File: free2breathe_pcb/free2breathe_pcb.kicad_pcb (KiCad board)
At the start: 2 copper layers, 98 parts, among them J1 LED_Connector, J2 Alarm_Connector, J3 USB4110-GF-A_REVB, Q1 DMN3404L, Q2 AO3401A, SW1 Power_Switch, U1 IP5328, U2 MCP6044-E/P, U3 CO Sensor, U4 MCP6044-E/P, U5 SO2 Sensor, U6 MCP6044-E/P, U7 O3 Sensor, U8 MCP6044-E/P, U9 NO2 Sensor

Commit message: group sensors with supporting hardware
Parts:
- removed D9: LED, LED_SMD:LED_0603_1608Metric
- removed the R8 at (89.7, 96.5)
- D1, D2, D3, D4: footprint LED_THT:LED_D4.0mm -> LED_THT:LED_D3.0mm
- D5: renamed from D7; footprint LED_SMD:LED_0603_1608Metric -> LED_THT:LED_D3.0mm
- D6: renamed from D8; footprint LED_SMD:LED_0603_1608Metric -> LED_THT:LED_D3.0mm
- D7: renamed from D5; footprint LED_SMD:LED_0603_1608Metric -> LED_THT:LED_D3.0mm
- D8: renamed from D6; footprint LED_SMD:LED_0603_1608Metric -> LED_THT:LED_D3.0mm
- moved R22 131.9 mm to (191.4, 151.5), turned to -90 degrees
- moved BT3 129.7 mm to (148.5, 156.9)
- moved R20 127.2 mm to (191.4, 155.3), turned to -90 degrees
- moved R15 117.8 mm to (191.4, 147.7), turned to -90 degrees
- moved R19 114.1 mm to (258.5, 159.1), turned to 90 degrees
- moved R18 110.9 mm to (210.4, 159.5), turned to 90 degrees
- moved R21 105.9 mm to (240.2, 155.7), turned to -90 degrees
- moved R17 105.0 mm to (240.2, 147.5), turned to -90 degrees
- moved R34 104.6 mm to (192.4, 126.4), turned to -90 degrees
- moved R13 104.4 mm to (240.2, 152.0), turned to 90 degrees
- moved R29 104.1 mm to (192.2, 117.8), turned to 90 degrees
- moved R16 101.9 mm to (244.8, 147.5), turned to -90 degrees
- moved C24 101.5 mm to (196.0, 151.5), turned to 90 degrees
- moved R14 99.1 mm to (258.3, 141.3), turned to -90 degrees
- moved R31 98.2 mm to (211.6, 127.9), turned to 90 degrees
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- renumbered C2 to C1, C14 to C10, C16 to C11, C8 to C12, C1 to C13, C11 to C14, C13 to C15, C15 to C16, C25 to C18, C24 to C19, C5 to C2, C18 to C21, C23 to C22, C22 to C23, C21 to C24, C32 to C25, C33 to C27, C30 to C29, C6 to C3, C27 to C30, C29 to C32, C3 to C4, C4 to C5, C7 to C6, C9 to C7, C10 to C8, C12 to C9, J3 to J1, J1 to J2, J2 to J3, Q2 to Q1, Q1 to Q2, R9 to R10, R4 to R11, R27 to R12, R12 to R13, R26 to R14, R16 to R15, R14 to R16, R13 to R17, R25 to R18, R20 to R19, R3 to R2, R19 to R20, R18 to R21, R17 to R22, R2 to R23, R10 to R24, R11 to R25, R42 to R26, R43 to R27, R34 to R28, R36 to R29, R5 to R3, R40 to R30, R41 to R31, R38 to R32, R35 to R33, R39 to R34, R37 to R35, R21 to R4, R22 to R5, R23 to R6, R24 to R8, R6 to R9, U4 to U2, U2 to U3, U5 to U4, U3 to U5
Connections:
- U1 pad 20: Net-(U1-Pad20) -> unconnected-(U1-Pad20)
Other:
- board outline added: 63.5 x 127 mm

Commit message: begin board layout
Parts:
- moved BT1 235.2 mm to (274.4, 83.1)
- moved SW1 227.3 mm to (246.3, 25.2), turned to -90 degrees
- moved BT2 176.6 mm to (274.5, 95.4)
- moved U1 175.4 mm to (247.0, 99.0), turned to -90 degrees
- moved C14 168.4 mm to (269.3, 99.4), turned to -90 degrees
- moved C15 166.0 mm to (267.5, 99.5), turned to -90 degrees
- moved C16 163.6 mm to (265.7, 99.5), turned to -90 degrees
- moved C17 161.3 mm to (263.9, 99.5), turned to -90 degrees
- moved D8 155.8 mm to (247.6, 119.7)
- moved L1 155.6 mm to (258.4, 99.0), turned to 90 degrees
- moved C12 154.9 mm to (253.8, 101.0), turned to -90 degrees
- moved D7 153.5 mm to (244.7, 119.7), turned to 180 degrees
- moved BT3 152.5 mm to (274.4, 70.8)
- moved J1 151.7 mm to (221.2, 96.8), turned to -90 degrees
- moved D6 151.7 mm to (247.6, 114.7)
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
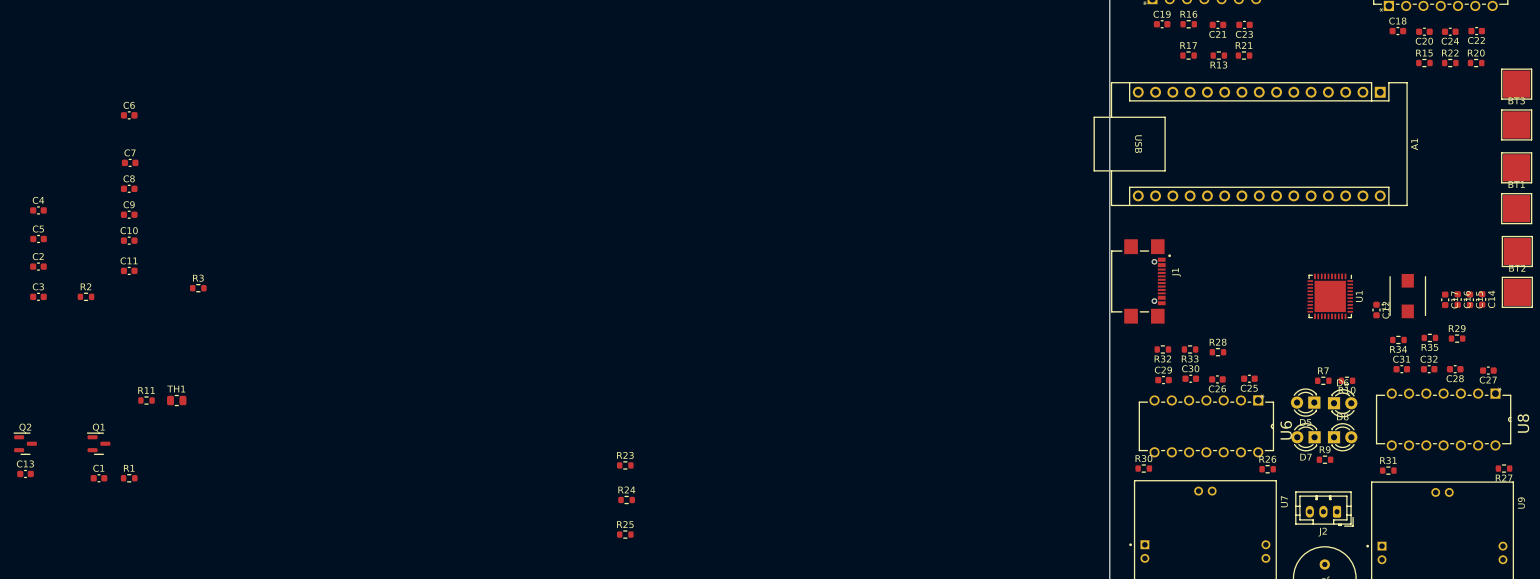
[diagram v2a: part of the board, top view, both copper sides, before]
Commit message: rest of components placed in board (very poorly)
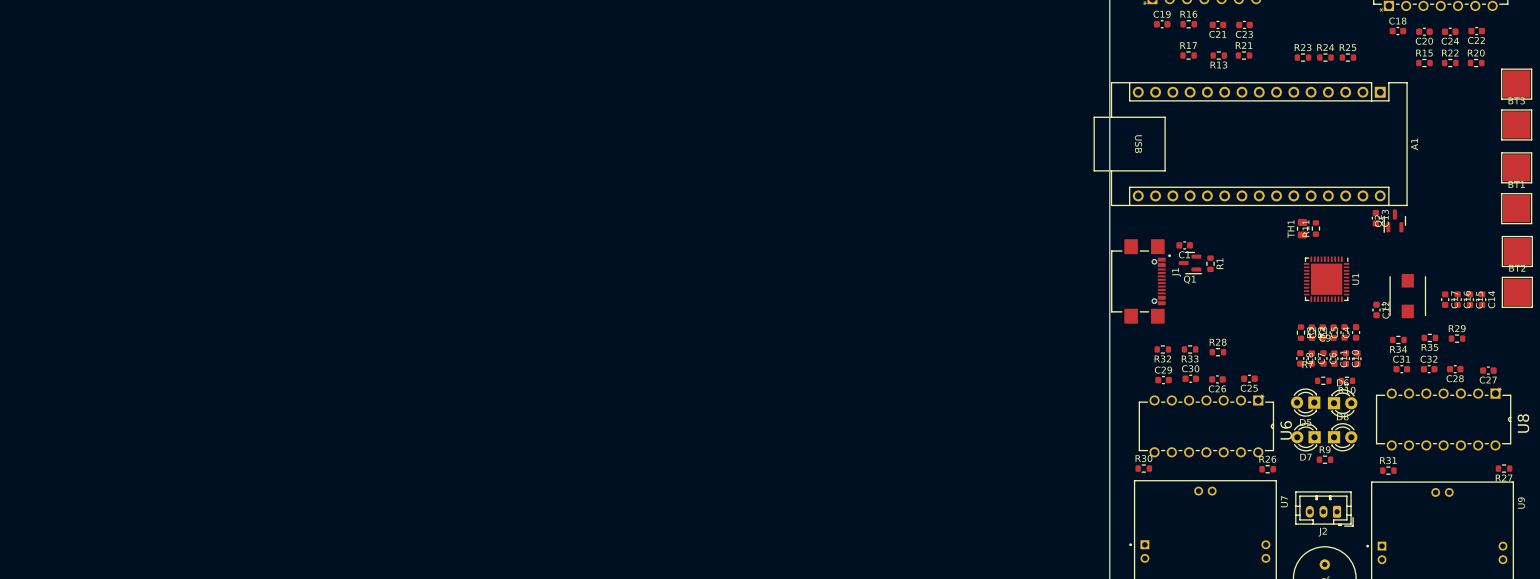
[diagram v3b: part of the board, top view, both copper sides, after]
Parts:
- moved Q2 203.9 mm to (256.5, 87.9), turned to 90 degrees
- moved C13 202.0 mm to (253.7, 87.5), turned to -90 degrees
- moved C4 194.5 mm to (250.8, 104.3), turned to 90 degrees
- moved C5 192.4 mm to (249.1, 104.3), turned to 90 degrees
- moved C3 190.4 mm to (247.5, 104.3), turned to 90 degrees
- moved C2 189.0 mm to (245.9, 104.3), turned to 90 degrees
- moved C9 181.8 mm to (251.0, 108.2), turned to -90 degrees
- moved R2 180.2 mm to (244.3, 104.3), turned to -90 degrees
- moved C10 179.7 mm to (249.3, 108.2), turned to -90 degrees
- moved C6 179.1 mm to (246.0, 108.1), turned to -90 degrees
- moved C11 177.6 mm to (247.6, 108.2), turned to -90 degrees
- moved C7 176.0 mm to (244.3, 108.1), turned to -90 degrees
- moved C8 173.9 mm to (242.6, 108.1), turned to -90 degrees
- moved R11 173.7 mm to (244.9, 89.0), turned to 90 degrees
- moved TH1 167.4 mm to (242.9, 89.0), turned to 90 degrees
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
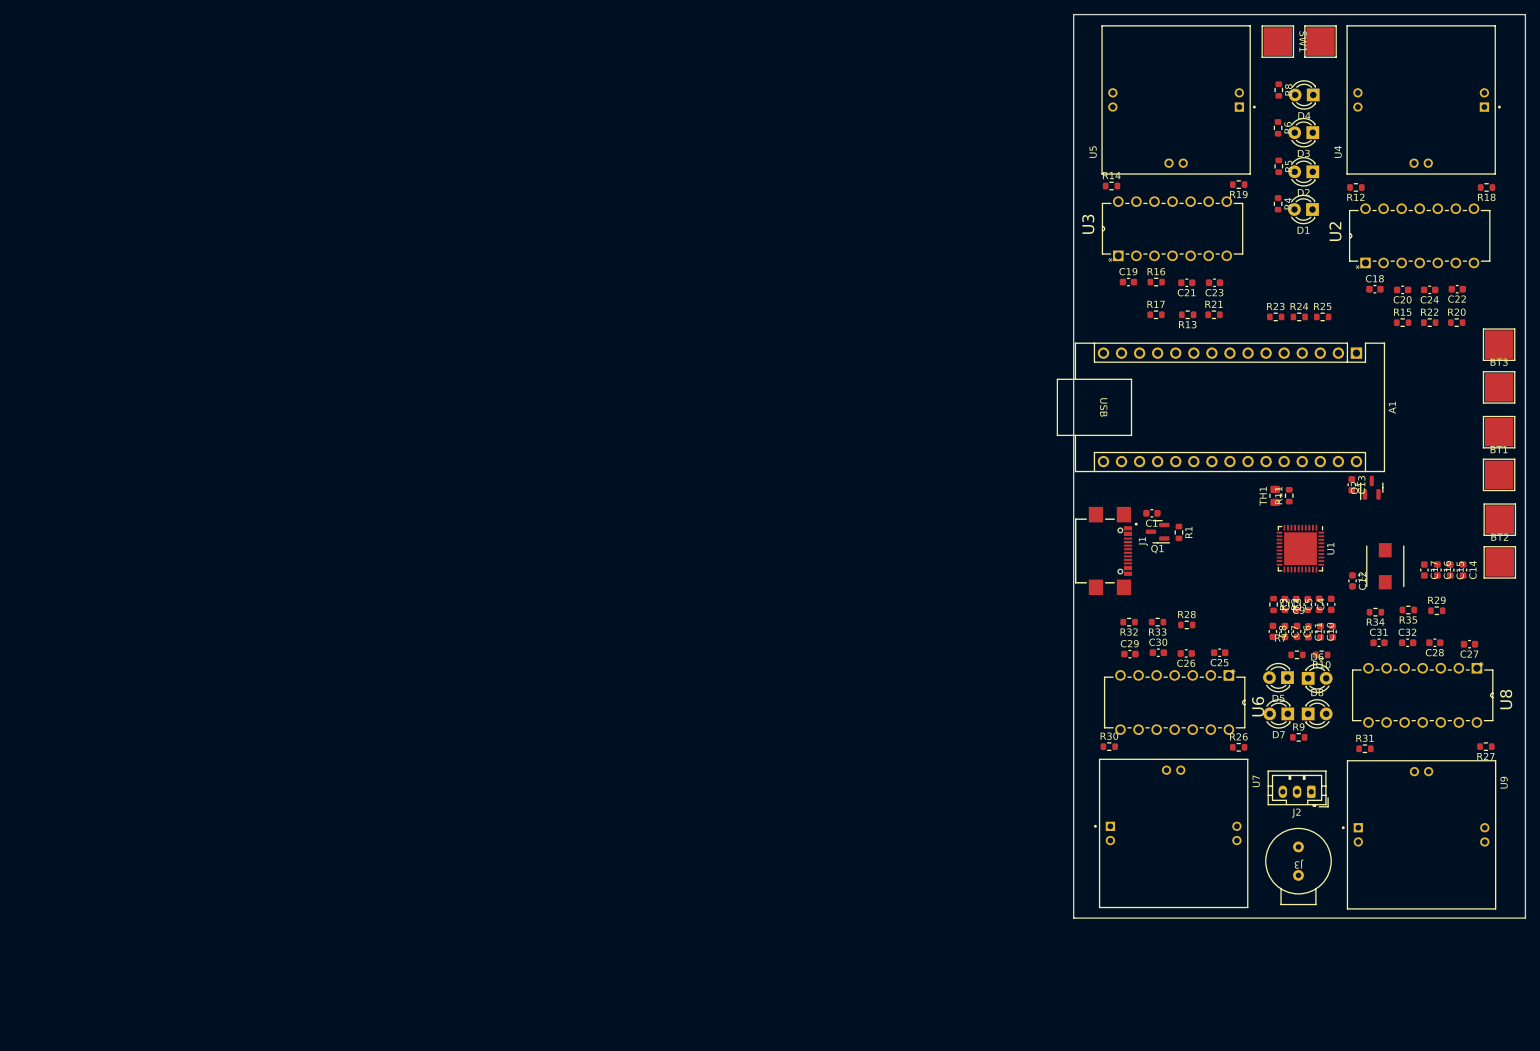
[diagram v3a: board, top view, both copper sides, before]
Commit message: add new PCB shape, move todo out of /src
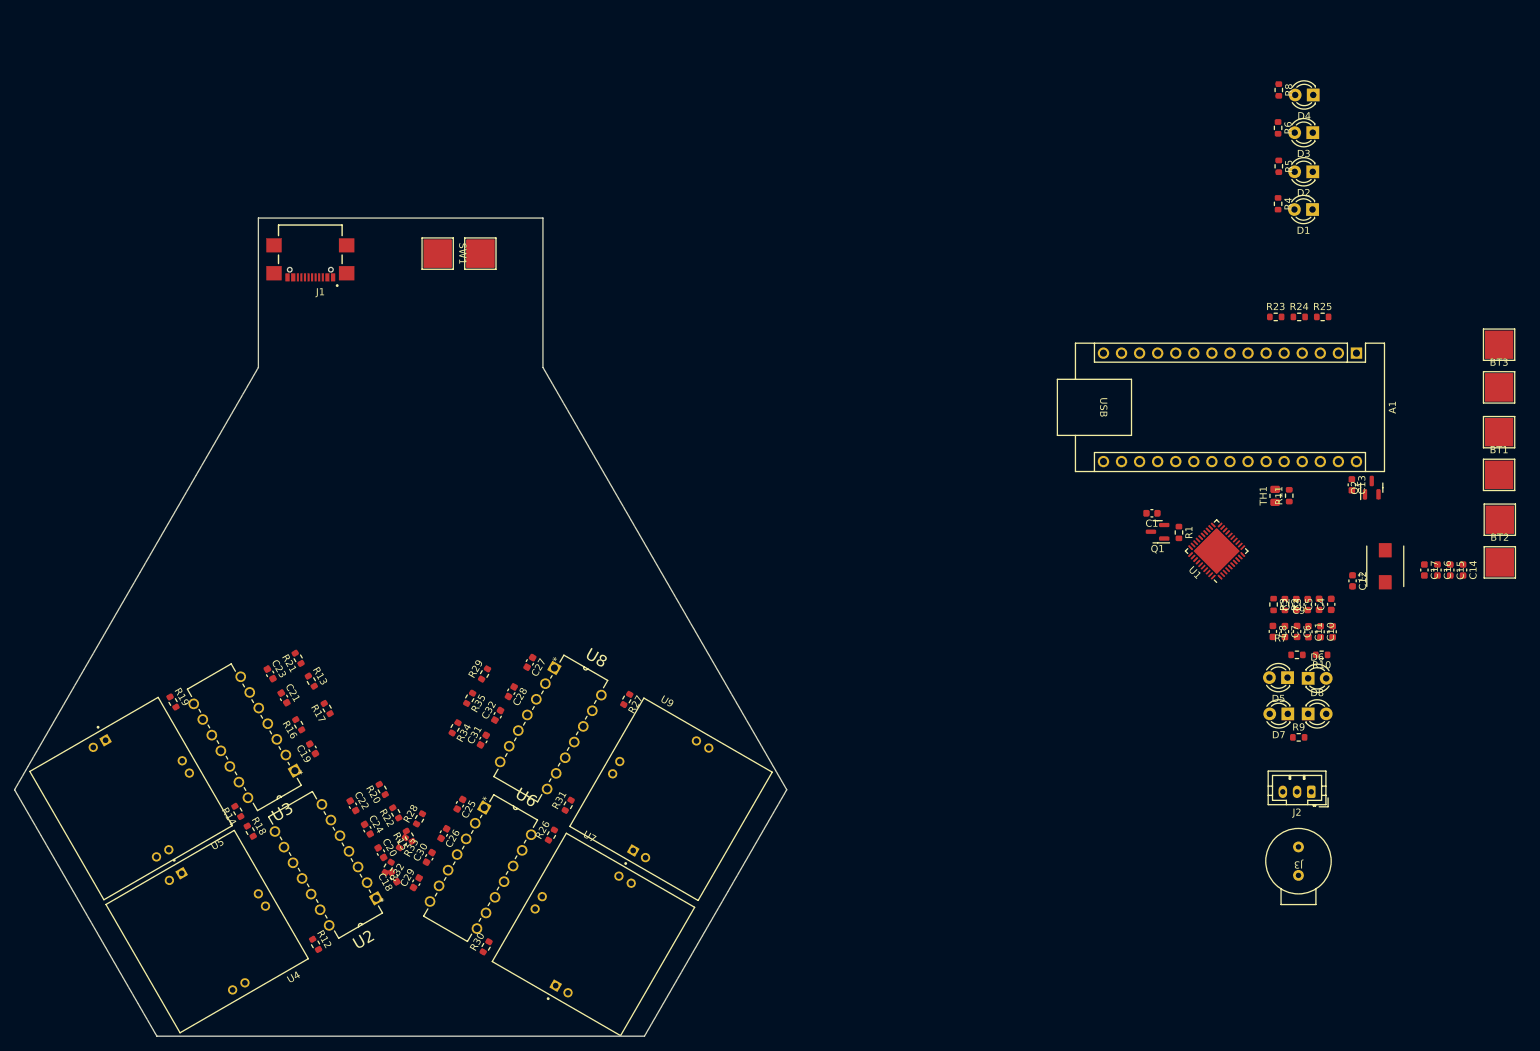
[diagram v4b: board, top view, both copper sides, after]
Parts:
- moved U4 206.8 mm to (92.8, 150.3), turned to -150 degrees
- moved R18 195.9 mm to (98.9, 136.2), turned to -60 degrees
- moved U2 189.9 mm to (102.3, 136.2), turned to -150 degrees
- moved R12 180.8 mm to (108.0, 152.1), turned to -60 degrees
- moved U5 176.7 mm to (82.1, 131.6), turned to -150 degrees
- moved C22 171.4 mm to (113.3, 132.6), turned to -60 degrees
- moved C24 167.5 mm to (115.3, 135.9), turned to -60 degrees
- moved R19 166.5 mm to (88.0, 118.0), turned to -60 degrees
- moved R20 164.7 mm to (117.4, 130.3), turned to 120 degrees
- moved C20 164.0 mm to (117.2, 139.2), turned to -60 degrees
- moved U3 161.5 mm to (90.9, 118.3), turned to -150 degrees
- moved R22 160.8 mm to (119.3, 133.6), turned to 120 degrees
- moved C18 160.7 mm to (119.1, 142.6), turned to 120 degrees
- moved R15 157.2 mm to (121.2, 136.9), turned to 120 degrees
- moved R14 151.0 mm to (97.1, 133.4), turned to 120 degrees
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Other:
- board size 63.5 x 127 mm -> 108.5 x 115 mm
